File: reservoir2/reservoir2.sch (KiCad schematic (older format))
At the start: 15 parts, among them J11 SMA, J12 SMA, J13 BNC, J21 SMA, J22 SMA, J23 BNC, J4 RESCONN, U1 Analog_ADUM1250, U2 JTD1524S3V3

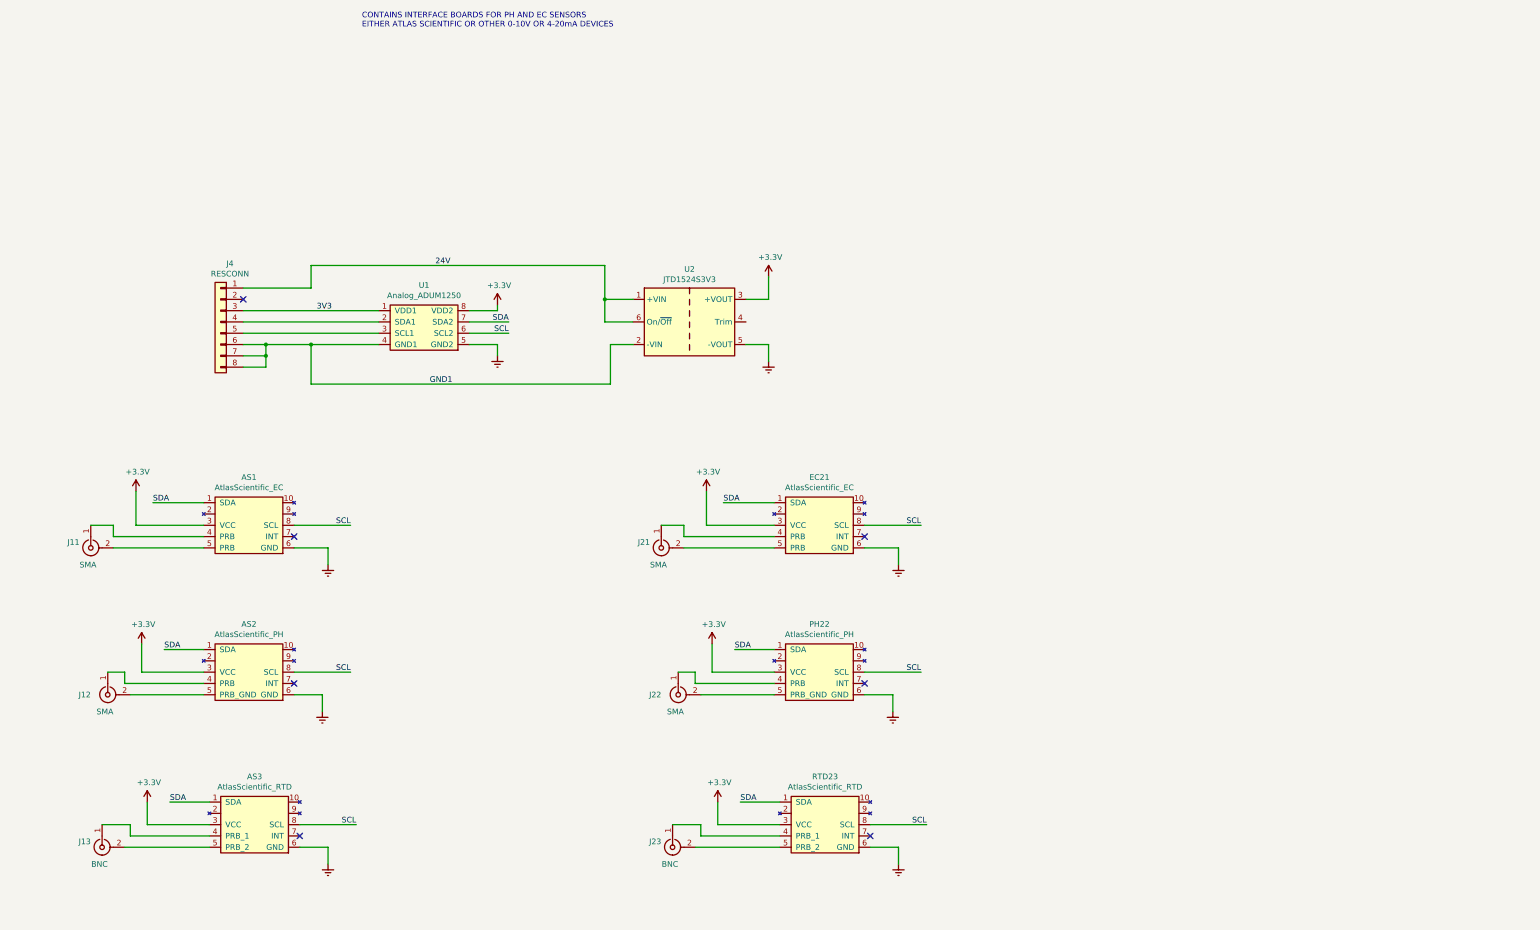
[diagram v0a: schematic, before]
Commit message: Added schematics following Atlas Scientific's recomended design.
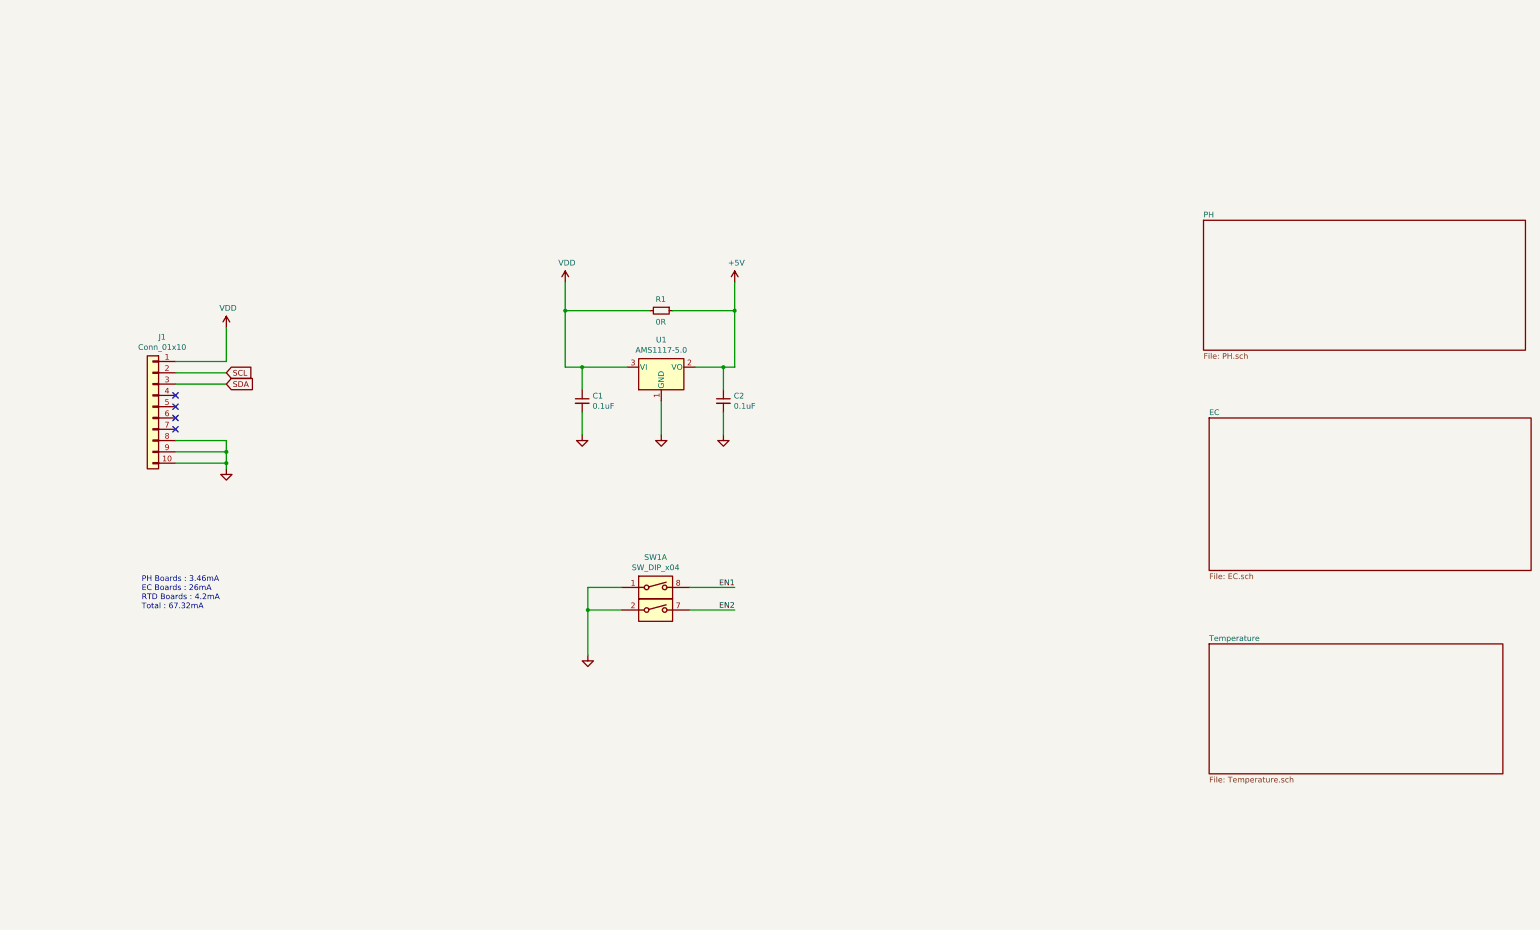
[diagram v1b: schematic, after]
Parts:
- removed AS1, EC21: AtlasScientific_EC, BCR_Langhe:AtlasScientific_OEM, symbol BCR:AtlasScientific_EC
- removed AS2, PH22: AtlasScientific_PH, BCR_Langhe:AtlasScientific_OEM, symbol BCR:AtlasScientific_PH
- removed AS3, RTD23: AtlasScientific_RTD, BCR_Langhe:AtlasScientific_OEM, symbol BCR:AtlasScientific_RTD
- removed J11, J12, J21, J22: SMA, symbol Connector:Conn_Coaxial
- removed J13, J23: BNC, symbol Connector:Conn_Coaxial
- removed J4: RESCONN, symbol Connector_Generic:Conn_01x08
- removed U1: Analog_ADUM1250, symbol BCR:Analog_ADUM1250
- removed U2: JTD1524S3V3, Converter_DCDC:Converter_DCDC_XP_POWER_JTDxxxxxxx_THT, symbol Converter_DCDC:JTD1524S3V3
- added C1, C2: 0.1uF, Capacitor_SMD:C_0805_2012Metric, symbol Device:C_Small
- added J1: Conn_01x10, Connector_PinHeader_2.54mm:PinHeader_1x10_P2.54mm_Vertical, symbol Connector_Generic:Conn_01x10
- added R1: 0R, Resistor_SMD:R_0805_2012Metric, symbol Device:R_Small
- added SW1: SW_DIP_x04, symbol BCR:SW_DIP_x04
- added U1: AMS1117-5.0, Package_TO_SOT_SMD:SOT-223-3_TabPin2, symbol Regulator_Linear:AMS1117-5.0
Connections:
- net SCL: now also J1.2 (Pin_2)
- net SDA: now also J1.3 (Pin_3)
- new net +5V: C2.1, R1.1, U1.2 (VO)
- new net EN1: SW1.8
- new net EN2: SW1.7
- new net GND: C1.2, C2.2, J1.10 (Pin_10), J1.8 (Pin_8), J1.9 (Pin_9), SW1.1, SW1.2, U1.1 (GND)
- new net VDD: C1.1, J1.1 (Pin_1), R1.2, U1.3 (VI)
- no-connect marks 7 -> 4
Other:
- note added: "PH Boards : 3.46mA\nEC Boards : 26mA\nRTD Boards : 4.2mA\nTotal : 67.32mA"
- note removed: "CONTAINS INTERFACE BOARDS FOR PH AND EC SENSORS\nEITHER ATLAS SCIENTIFIC OR OTHER 0-10V OR 4-20mA DEVICES"

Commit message: Created new board design for connected grounds.
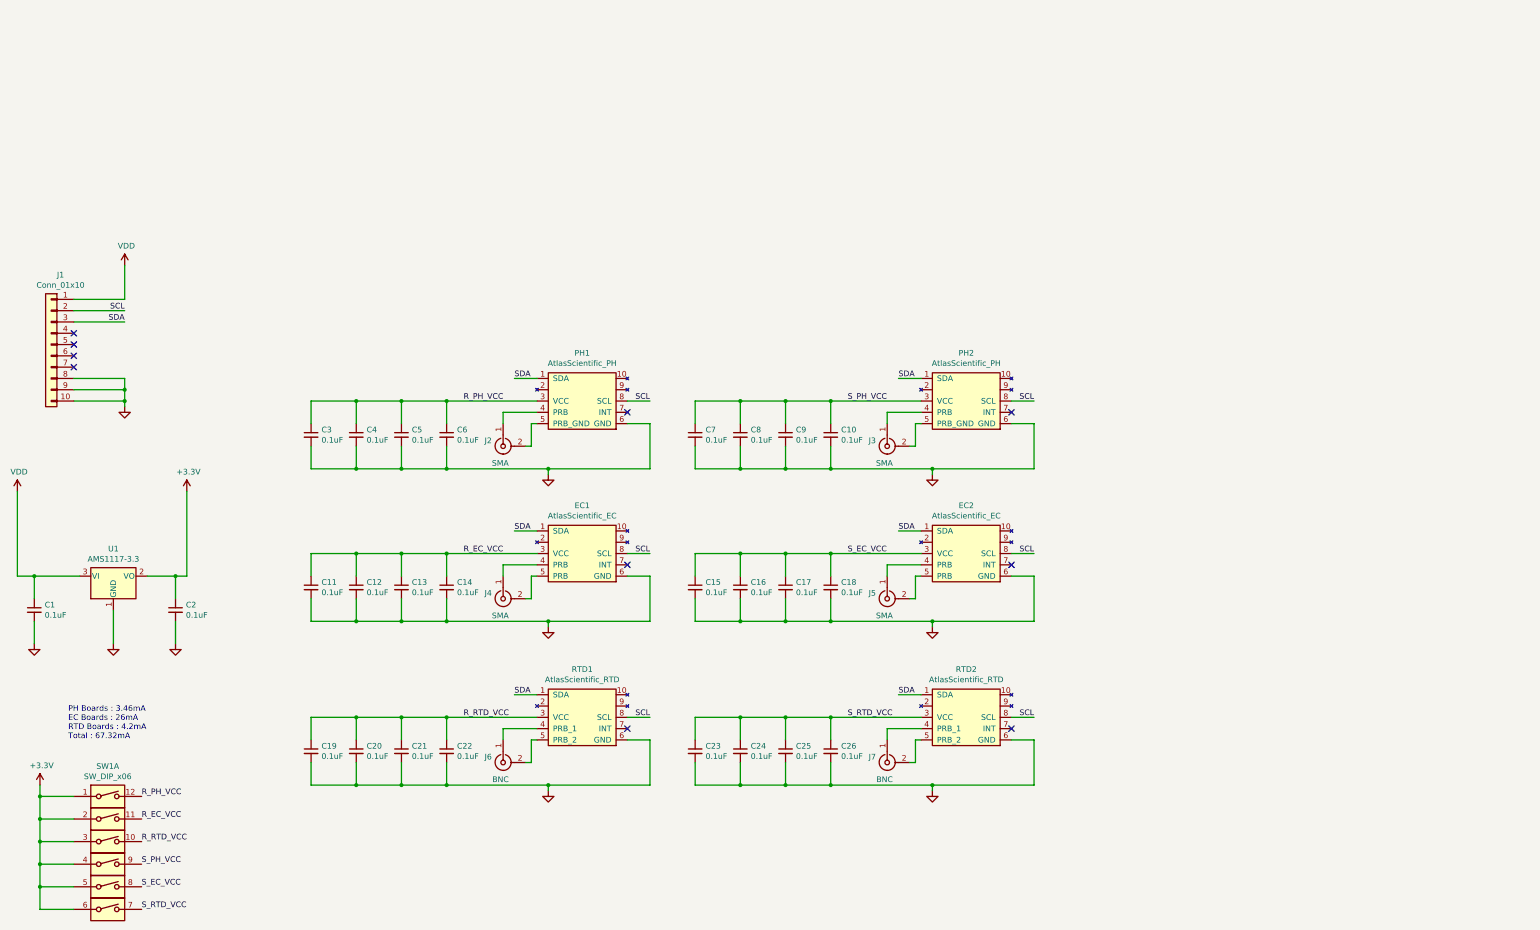
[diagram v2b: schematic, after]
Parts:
- removed R1: 0R, Resistor_SMD:R_0805_2012Metric, symbol Device:R_Small
- removed SW1: SW_DIP_x04, symbol BCR:SW_DIP_x04
- added C10, C11, C12, C13, C14, C15, C16, C17, C18, C19, C20, C21, C22, C23, C24, C25, C26, C3, C4, C5, C6, C7, C8, C9: 0.1uF, Capacitor_SMD:C_0805_2012Metric, symbol Device:C_Small
- added EC1, EC2: AtlasScientific_EC, BCR_Langhe:AtlasScientific_OEM, symbol BCR:AtlasScientific_EC
- added J2, J3, J4, J5: SMA, BCR_Connector:SMA_EdgeMount, symbol Connector:Conn_Coaxial
- added J6, J7: BNC, BCR_Connector:Molex_BNC_Jack_73100, symbol Connector:Conn_Coaxial
- added PH1, PH2: AtlasScientific_PH, BCR_Langhe:AtlasScientific_OEM, symbol BCR:AtlasScientific_PH
- added RTD1, RTD2: AtlasScientific_RTD, BCR_Langhe:AtlasScientific_OEM, symbol BCR:AtlasScientific_RTD
- added SW1: SW_DIP_x06, BCR_Switch:Cixi_SMD_DIP_Switch_6, symbol BCR:SW_DIP_x06
- C1, C2: LCSC (none) -> C49678
- U1: value AMS1117-5.0 -> AMS1117-3.3; LCSC (none) -> C6186
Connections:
- net GND: now also C10.2, C11.2, C12.2, C13.2, C14.2, C15.2, C16.2, C17.2, C18.2, C19.2, C20.2, C21.2, C22.2, C23.2, C24.2, C25.2, C26.2, C3.2, C4.2, C5.2, C6.2, C7.2, C8.2, C9.2, EC1.6 (GND), EC2.6 (GND), PH1.6 (GND), PH2.6 (GND), RTD1.6 (GND), RTD2.6 (GND)
- net SCL: now also EC1.8 (SCL), EC2.8 (SCL), PH1.8 (SCL), PH2.8 (SCL), RTD1.8 (SCL), RTD2.8 (SCL)
- net SDA: now also EC1.1 (SDA), EC2.1 (SDA), PH1.1 (SDA), PH2.1 (SDA), RTD1.1 (SDA), RTD2.1 (SDA)
- net +5V renamed +3V3
- net +3V3: now also SW1.1, SW1.2, SW1.3, SW1.4, SW1.5, SW1.6
- new net: J2.1 (In), PH1.4 (PRB)
- new net: J2.2 (Ext), PH1.5 (PRB_GND)
- new net: J3.1 (In), PH2.4 (PRB)
- new net: J3.2 (Ext), PH2.5 (PRB_GND)
- new net: EC1.4 (PRB), J4.1 (In)
- new net: EC1.5 (PRB), J4.2 (Ext)
- new net: EC2.4 (PRB), J5.1 (In)
- new net: EC2.5 (PRB), J5.2 (Ext)
- new net: J6.1 (In), RTD1.4 (PRB_1)
- new net: J6.2 (Ext), RTD1.5 (PRB_2)
- new net: J7.1 (In), RTD2.4 (PRB_1)
- new net: J7.2 (Ext), RTD2.5 (PRB_2)
- new net R_EC_VCC: C11.1, C12.1, C13.1, C14.1, EC1.3 (VCC), SW1.11
- new net R_PH_VCC: C3.1, C4.1, C5.1, C6.1, PH1.3 (VCC), SW1.12
- new net R_RTD_VCC: C19.1, C20.1, C21.1, C22.1, RTD1.3 (VCC), SW1.10
- new net S_EC_VCC: C15.1, C16.1, C17.1, C18.1, EC2.3 (VCC), SW1.8
- new net S_PH_VCC: C10.1, C7.1, C8.1, C9.1, PH2.3 (VCC), SW1.9
- new net S_RTD_VCC: C23.1, C24.1, C25.1, C26.1, RTD2.3 (VCC), SW1.7
- no-connect marks 4 -> 10
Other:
- moved on the sheet: C1, C2, J1, U1
